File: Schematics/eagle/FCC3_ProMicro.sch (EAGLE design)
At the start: 9 parts, among them IC1 MCP3202P

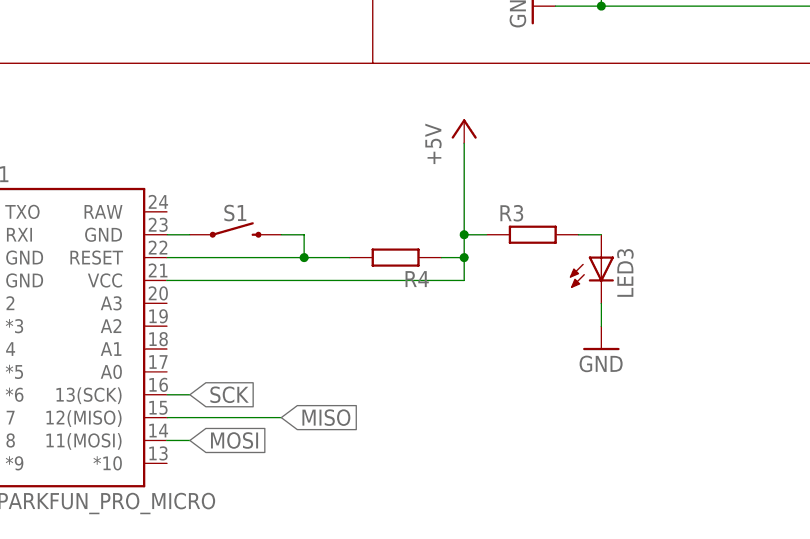
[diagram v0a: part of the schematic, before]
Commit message: replace force mapping with Analog/Digital FLCS
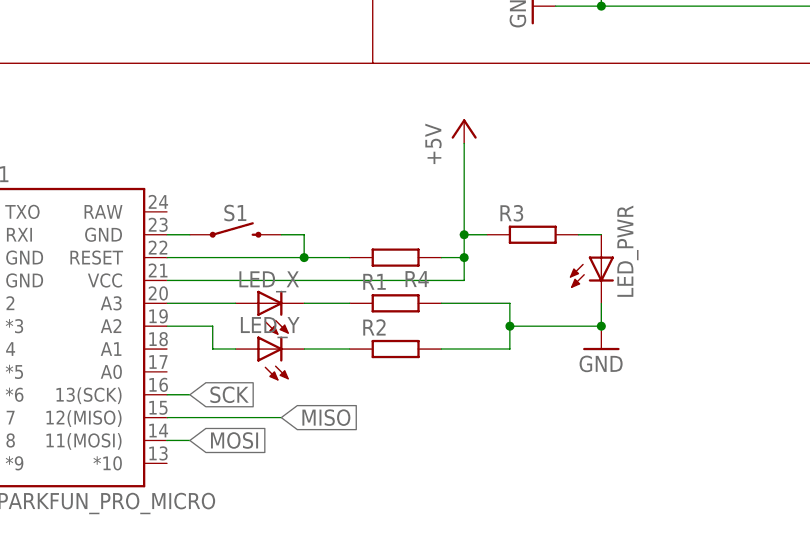
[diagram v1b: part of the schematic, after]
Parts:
- removed LED3: (no value), led:LED5MM
- added LED_PWR, LED_X, LED_Y: (no value), led:LED3MM
- added R1, R2: (no value), resistor:R-EU_0204/5
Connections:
- new net N$3: B1.A3, LED_X.A
- new net N$4: B1.A2, LED_Y.A
- new net N$6: LED_Y.C, R2.1
- new net N$7: LED_X.C, R1.1
- net GND: now also LED_PWR.C, R1.2, R2.2; no longer LED3.C
- net N$5: now also LED_PWR.A; no longer LED3.A
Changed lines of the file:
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@@
 <part name="U$2" library="uriba" deviceset="JST_EH_3PIN" device=""/>
 <part name="U$3" library="uriba" deviceset="JST_EH_5PIN" device=""/>
-<part name="LED3" library="led" deviceset="LED" device="5MM"/>
+<part name="LED_PWR" library="led" deviceset="LED" device="3MM"/>
 <part name="S1" library="SparkFun-Switches" deviceset="MOMENTARY-SWITCH-SPST" device="-PTH-6.0MM"/>
 <part name="R3" library="resistor" deviceset="R-EU_" device="0204/5"/>
@@
 <part name="FRAME1" library="frames" deviceset="DINA5_L" device=""/>
 <part name="B1" library="SparkFun-Boards" deviceset="SPARKFUN_PRO_MICRO" device=""/>
+<part name="LED_X" library="led" deviceset="LED" device="3MM"/>
+<part name="LED_Y" library="led" deviceset="LED" device="3MM"/>
+<part name="R1" library="resistor" deviceset="R-EU_" device="0204/5"/>
+<part name="R2" library="resistor" deviceset="R-EU_" device="0204/5"/>
 </parts>
 <sheets>
@@
 <instance part="U$2" gate="G$1" x="167.64" y="111.76" rot="R90"/>
 <instance part="U$3" gate="G$1" x="58.42" y="101.6" rot="R90"/>
-<instance part="LED3" gate="G$1" x="109.22" y="53.34"/>
+<instance part="LED_PWR" gate="G$1" x="109.22" y="53.34"/>
 <instance part="S1" gate="G$1" x="68.58" y="55.88" smashed="yes">
 <attribute name="NAME" x="68.58" y="57.404" size="1.778" layer="95" font="vector" align="bottom-center"/>
@@
 <instance part="FRAME1" gate="G$1" x="0" y="0"/>
 <instance part="B1" gate="G$1" x="48.26" y="43.18"/>
+<instance part="LED_X" gate="G$1" x="71.12" y="48.26" rot="R90"/>
+<instance part="LED_Y" gate="G$1" x="71.12" y="43.18" rot="R90"/>
+<instance part="R1" gate="G$1" x="86.36" y="48.26"/>
+<instance part="R2" gate="G$1" x="86.36" y="43.18"/>
 </instances>
 <busses>
@@
 <pinref part="GND1" gate="1" pin="GND"/>
 <wire x1="109.22" y1="45.72" x2="109.22" y2="48.26" width="0.1524" layer="91"/>
-<pinref part="LED3" gate="G$1" pin="C"/>
+<pinref part="LED_PWR" gate="G$1" pin="C"/>
+<pinref part="R1" gate="G$1" pin="2"/>
+<wire x1="91.44" y1="48.26" x2="99.06" y2="48.26" width="0.1524" layer="91"/>
+<wire x1="99.06" y1="48.26" x2="99.06" y2="45.72" width="0.1524" layer="91"/>
+<wire x1="99.06" y1="45.72" x2="109.22" y2="45.72" width="0.1524" layer="91"/>
+<junction x="109.22" y="45.72"/>
+<pinref part="R2" gate="G$1" pin="2"/>
+<wire x1="91.44" y1="43.18" x2="99.06" y2="43.18" width="0.1524" layer="91"/>
+<wire x1="99.06" y1="43.18" x2="99.06" y2="45.72" width="0.1524" layer="91"/>
+<junction x="99.06" y="45.72"/>
 </segment>
 <segment>
@@
 <net name="N$5" class="0">
 <segment>
-<pinref part="LED3" gate="G$1" pin="A"/>
+<pinref part="LED_PWR" gate="G$1" pin="A"/>
 <pinref part="R3" gate="G$1" pin="2"/>
 <wire x1="106.68" y1="55.88" x2="109.22" y2="55.88" width="0.1524" layer="91"/>
@@
 </segment>
 </net>
+<net name="N$3" class="0">
+<segment>
+<pinref part="B1" gate="G$1" pin="A3"/>
+<pinref part="LED_X" gate="G$1" pin="A"/>
+<wire x1="60.96" y1="48.26" x2="68.58" y2="48.26" width="0.1524" layer="91"/>
+</segment>
+</net>
+<net name="N$4" class="0">
+<segment>
+<pinref part="B1" gate="G$1" pin="A2"/>
+<wire x1="60.96" y1="45.72" x2="66.04" y2="45.72" width="0.1524" layer="91"/>
+<pinref part="LED_Y" gate="G$1" pin="A"/>
+<wire x1="66.04" y1="45.72" x2="66.04" y2="43.18" width="0.1524" layer="91"/>
+<wire x1="66.04" y1="43.18" x2="68.58" y2="43.18" width="0.1524" layer="91"/>
+</segment>
+</net>
+<net name="N$6" class="0">
+<segment>
+<pinref part="LED_Y" gate="G$1" pin="C"/>
+<pinref part="R2" gate="G$1" pin="1"/>
+<wire x1="76.2" y1="43.18" x2="81.28" y2="43.18" width="0.1524" layer="91"/>
+</segment>
+</net>
+<net name="N$7" class="0">
+<segment>
+<pinref part="LED_X" gate="G$1" pin="C"/>
+<pinref part="R1" gate="G$1" pin="1"/>
+<wire x1="76.2" y1="48.26" x2="81.28" y2="48.26" width="0.1524" layer="91"/>
+</segment>
+</net>
